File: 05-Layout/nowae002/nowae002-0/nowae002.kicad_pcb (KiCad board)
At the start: 2 copper layers, 40 x 16 mm, 54 parts, among them J1 SMALL_JUMPER, J2 SMALL_JUMPER, P1 USB_A_90, Q1 IRLML6402, U1 FT230XQ, U2 TPS62152, U3 RN4870

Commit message: WiP: placement components (nowae002-0)
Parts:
- added J3: SMALL_JUMPER, MISC:JUMPERSMD-2, F.Cu at (20.0, 10.1)
- added R22: 4k7, RESISTOR:RESISTOR-0402, F.Cu at (20.0, 10.1)
- P1: footprint CONNECTOR:USB-A-PLUG-SMD -> CONNECTOR:USB-A-WURTH-629004113921
- moved P1 245.0 mm to (-5.65, -8.00)
- moved R18 244.6 mm to (20.6, -8.20)
- moved C1 244.1 mm to (7.45, -6.25)
- moved C2 244.1 mm to (7.45, -9.75)
- moved C4 244.1 mm to (9.85, -1.60)
- moved C5 244.1 mm to (9.85, -3.70)
- moved C6 244.1 mm to (12.2, -1.90)
- moved C7 244.1 mm to (9.95, -5.90)
- moved J2 244.1 mm to (24.2, -18.2)
- moved L1 244.1 mm to (15.2, -2.85)
- moved R1 244.1 mm to (7.45, -7.00)
- moved R2 244.1 mm to (7.45, -9.00)
- moved R3 244.1 mm to (12.1, -8.15)
- moved R8 244.1 mm to (14.6, -0.80)
- moved C3 244.1 mm to (9.80, -9.50)
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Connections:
- net /RX renamed /UART_RX
- net /TX renamed /UART_TX
- net Net-(J1-Pad1) renamed /RESET
- U1 pad 16: Net-(U1-Pad16) -> /UART_RTS
- U1 pad 4: Net-(U1-Pad4) -> /UART_CTS
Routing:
- net /LINK_DROP: track 0.00 -> 6.64 mm, vias 0 -> 1
- net /RSSI_IND: track 0.00 -> 5.43 mm, vias 0 -> 1
- net /PWM1: track 0.00 -> 4.36 mm, vias 0 -> 1
- net /PAIRING_KEY: track 0.00 -> 3.95 mm, vias 0 -> 1
- net GND: track 18.8 -> 22.5 mm, vias 9 -> 21
- net /P3_5: track 0.00 -> 3.68 mm, vias 0 -> 1
- net /BATTERY_IND: track 0.00 -> 3.52 mm, vias 0 -> 1
- net /ON/OFF: track 0.00 -> 3.35 mm, vias 0 -> 1
- net /P2_4: track 0.00 -> 2.18 mm, vias 0 -> 1
- net /STATUS1_IND: track 0.00 -> 2.13 mm, vias 0 -> 1
- net /P1_2: track 0.00 -> 1.80 mm, vias 0 -> 1
- net /STATUS2_IND: track 0.00 -> 1.75 mm, vias 0 -> 1
- net (no net): track 0.00 -> 1.75 mm, vias 0 -> 1
- net /PWM2: track 0.00 -> 1.55 mm, vias 0 -> 1
- net /P1_3: track 0.00 -> 1.55 mm, vias 0 -> 1
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
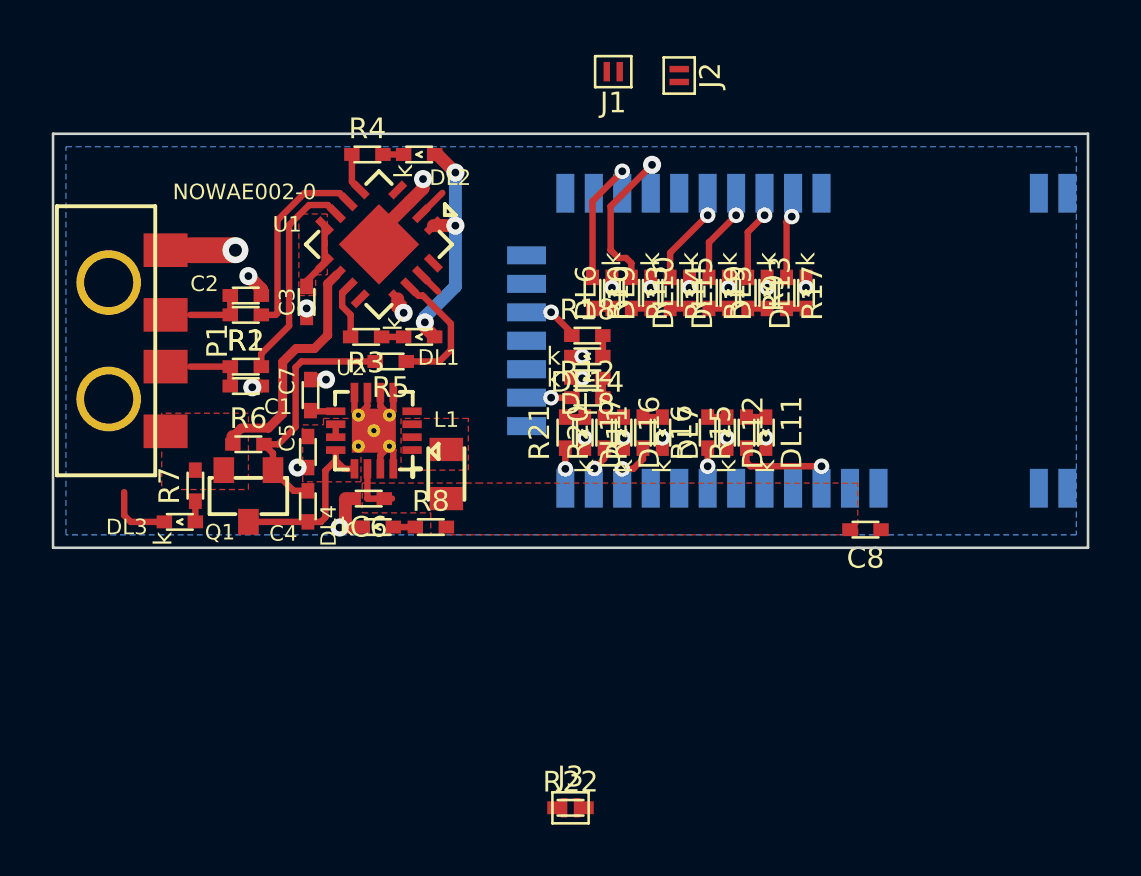
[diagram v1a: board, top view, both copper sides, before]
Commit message: WiP: placement wires (nowae002-0)
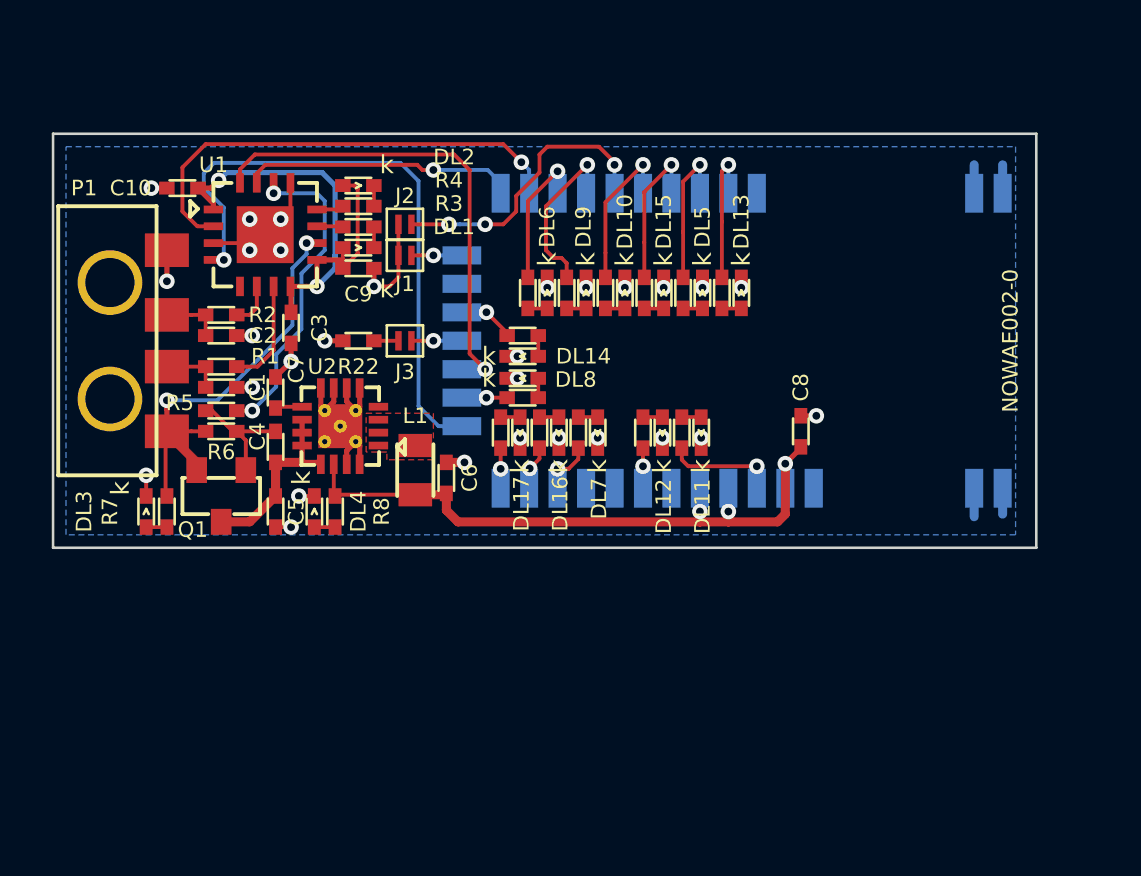
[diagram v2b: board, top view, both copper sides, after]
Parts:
- added C10: 100nF, CAPACITOR:CAPACITOR-0402, F.Cu at (5.00, -13.9)
- added C9: 100nF, CAPACITOR:CAPACITOR-0402, F.Cu at (11.8, -10.8)
- moved R22 19.8 mm to (11.8, -8.00), turned to 180 degrees
- moved J3 19.2 mm to (13.6, -8.00), turned to 180 degrees
- moved J2 12.1 mm to (13.6, -12.5), turned to 180 degrees
- moved J1 10.7 mm to (13.6, -11.3)
- moved R5 6.82 mm to (6.50, -5.30)
- moved C8 4.55 mm to (28.9, -4.50), turned to 270 degrees
- moved U1 4.41 mm to (8.20, -12.1), turned to 0 degrees
- moved R3 4.26 mm to (11.8, -12.4)
- moved DL1 4.17 mm to (11.8, -11.6), turned to 0 degrees
- moved R8 3.75 mm to (10.9, -1.40), turned to 90 degrees
- moved C6 3.10 mm to (15.2, -2.70), turned to 90 degrees
- moved DL2 2.64 mm to (11.8, -14.0), turned to 0 degrees
- moved C5 2.62 mm to (8.60, -1.40)
- moved C4 2.62 mm to (8.60, -3.90)
- moved DL4 2.52 mm to (10.1, -1.40), turned to 90 degrees
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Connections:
- U1 pad 12: Net-(U1-Pad12) -> Net-(R4-Pad1)
- U1 pad 5: Net-(R4-Pad1) -> Net-(U1-Pad5)
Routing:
- net +3.3V: track 2.10 -> 26.0 mm, vias 0 -> 3
- net /UART_CTS: track 0.00 -> 23.5 mm, vias 0 -> 1
- net /UART_RTS: track 0.00 -> 18.7 mm, vias 0 -> 1
- net /UART_RX: track 1.14 -> 18.2 mm, vias 0 -> 1
- net /UART_RX_IND: track 0.00 -> 11.3 mm, vias 0 -> 3
- net /UART_TX: track 0.91 -> 10.6 mm, vias 0 -> 1
- net GND: track 22.5 -> 31.1 mm, vias 21 -> 29
- net /VCCIO: track 11.6 -> 19.8 mm, vias 3 -> 2
- net +5V: track 9.23 -> 17.1 mm, vias 0 -> 2
- net /EN_PWR: track 5.11 -> 12.4 mm, vias 0 -> 2
- net Net-(R2-Pad1): track 7.55 -> 1.71 mm
- net Net-(C4-Pad2): track 9.80 -> 4.68 mm
- net Net-(R1-Pad2): track 8.21 -> 4.16 mm
- net /P3_5: track 3.68 -> 5.88 mm
- net /ON/OFF: track 3.35 -> 5.55 mm
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- removed copper zone on F.Cu, net +3.3V
- removed copper zone on F.Cu, net +5V
- removed copper zone on F.Cu, net /VCCIO
- removed copper zone on F.Cu, net Net-(C4-Pad1)
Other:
- board size 40 x 16 mm -> 38 x 16 mm
- net class Default: trace_width 0.25 -> 0.15; via_dia 0.7 -> 0.6
- rule trace_min: 0.2 -> 0.15
- rule via_min_size: 0.3 -> 0.5

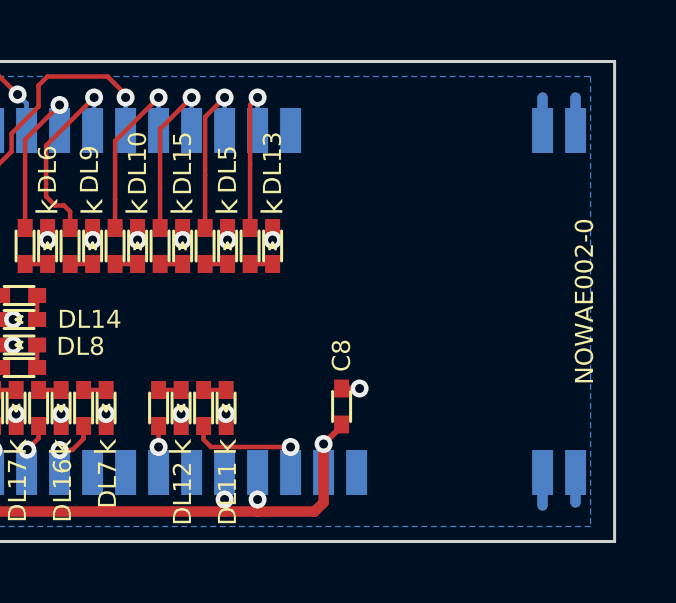
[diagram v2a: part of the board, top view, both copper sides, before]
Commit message: Added logos. (nowae002-0) Updated U3 footprint. (nowae002-0)
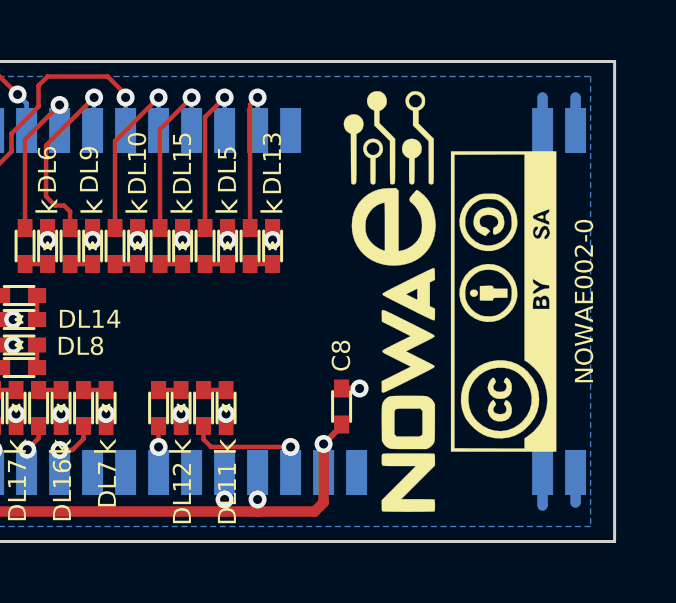
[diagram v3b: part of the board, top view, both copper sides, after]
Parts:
- added G***: LOGO, LOGO:LOGO_NOWAE_15MM_FSILK, F.Cu at (30.5, -8.00)
- added G***: LOGO, LOGO:LOGO_CC-BY-SA_10MM_FSILK, F.Cu at (34.3, -8.00)
- added G***: LOGO, LOGO:LOGO_OSH_10MM_FSILK, B.Cu at (8.60, -8.00)

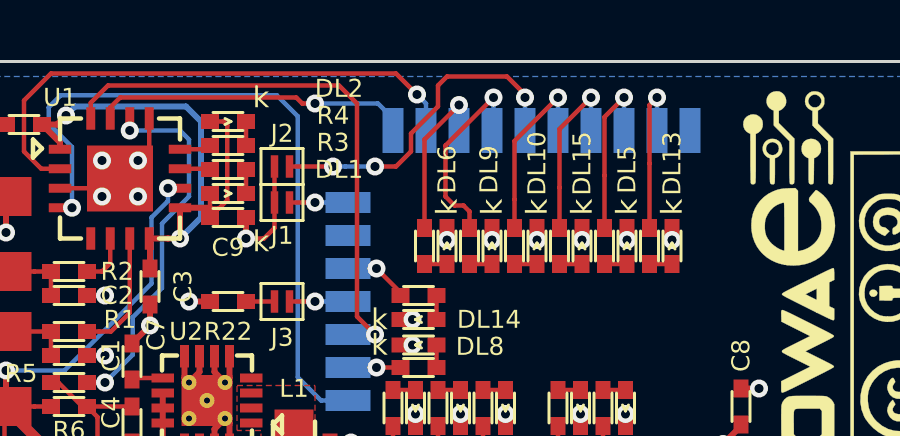
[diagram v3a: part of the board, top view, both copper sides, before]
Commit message: WiP: placement wires (nowae002-0)
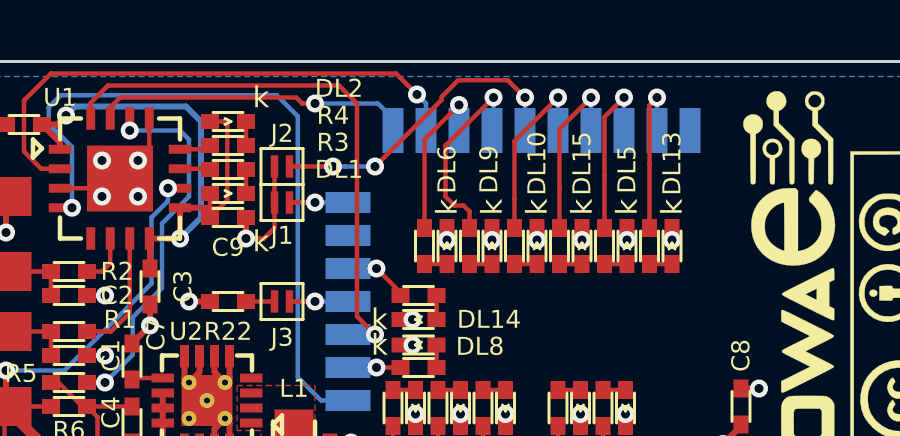
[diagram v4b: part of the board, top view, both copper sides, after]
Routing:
- net /UART_RX_IND: track 11.3 -> 10.4 mm
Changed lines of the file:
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@@
     (links 128)
     (no_connects 0)
-    (area -15.325001 -16.050001 38.125001 0.304762)
+    (area -0.050001 -16.050001 38.050001 0.050001)
     (thickness 1.2)
     (drawings 5)
-    (tracks 339)
+    (tracks 336)
     (zones 0)
     (modules 61)
@@
   (segment (start 18.8 -5.05) (end 19.55 -5.05) (width 0.15) (layer F.Cu) (net 30))
   (segment (start 18.05 -5.05) (end 17.3 -5.05) (width 0.15) (layer F.Cu) (net 31))
-  (segment (start 17.9 -13) (end 17.4 -12.5) (width 0.15) (layer F.Cu) (net 32))
-  (segment (start 17.4 -12.5) (end 16.7 -12.5) (width 0.15) (layer F.Cu) (net 32))
-  (segment (start 17.9 -13.6) (end 18.8 -14.5) (width 0.15) (layer F.Cu) (net 32))
-  (segment (start 17.9 -13.6) (end 17.9 -13) (width 0.15) (layer F.Cu) (net 32))
+  (segment (start 16.7 -12.5) (end 18.924999 -14.724999) (width 0.15) (layer F.Cu) (net 32))
+  (segment (start 19.473999 -15.375001) (end 21.124999 -15.375001) (width 0.15) (layer F.Cu) (net 32))
+  (segment (start 18.924999 -14.724999) (end 18.924999 -14.826001) (width 0.15) (layer F.Cu) (net 32))
+  (segment (start 21.124999 -15.375001) (end 21.400001 -15.099999) (width 0.15) (layer F.Cu) (net 32))
+  (segment (start 18.924999 -14.826001) (end 19.473999 -15.375001) (width 0.15) (layer F.Cu) (net 32))
+  (segment (start 21.400001 -15.099999) (end 21.7 -14.8) (width 0.15) (layer F.Cu) (net 32))
   (segment (start 21.7 -14.8) (end 21.7 -13.7) (width 0.15) (layer B.Cu) (net 32))
-  (segment (start 21.1 -15.5) (end 21.7 -14.9) (width 0.15) (layer F.Cu) (net 32))
-  (segment (start 21.7 -14.9) (end 21.7 -14.8) (width 0.15) (layer F.Cu) (net 32))
   (via (at 21.7 -14.8) (size 0.6) (drill 0.3) (layers F.Cu B.Cu) (net 32))
-  (segment (start 19.1 -15.5) (end 21.1 -15.5) (width 0.15) (layer F.Cu) (net 32))
-  (segment (start 18.8 -15.2) (end 19.1 -15.5) (width 0.15) (layer F.Cu) (net 32))
-  (segment (start 18.8 -14.5) (end 18.8 -15.2) (width 0.15) (layer F.Cu) (net 32))
   (segment (start 15.724264 -12.5) (end 16.7 -12.5) (width 0.15) (layer B.Cu) (net 32))
   (via (at 16.7 -12.5) (size 0.6) (drill 0.3) (layers F.Cu B.Cu) (net 32))
